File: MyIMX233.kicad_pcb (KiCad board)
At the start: 2 copper layers, 74.1 x 92 mm, 82 parts, among them IC1 iMX233, IC2 DDR_SDRAM_MT46_x16, J1 USB_OTG, P1 4p2, P2 1v2, P3 VDDA1v8, P4 2v5, P5 3v3, P6 1v, SW1 SWITCH_PUSHBUTTON, Y1 24Mhz

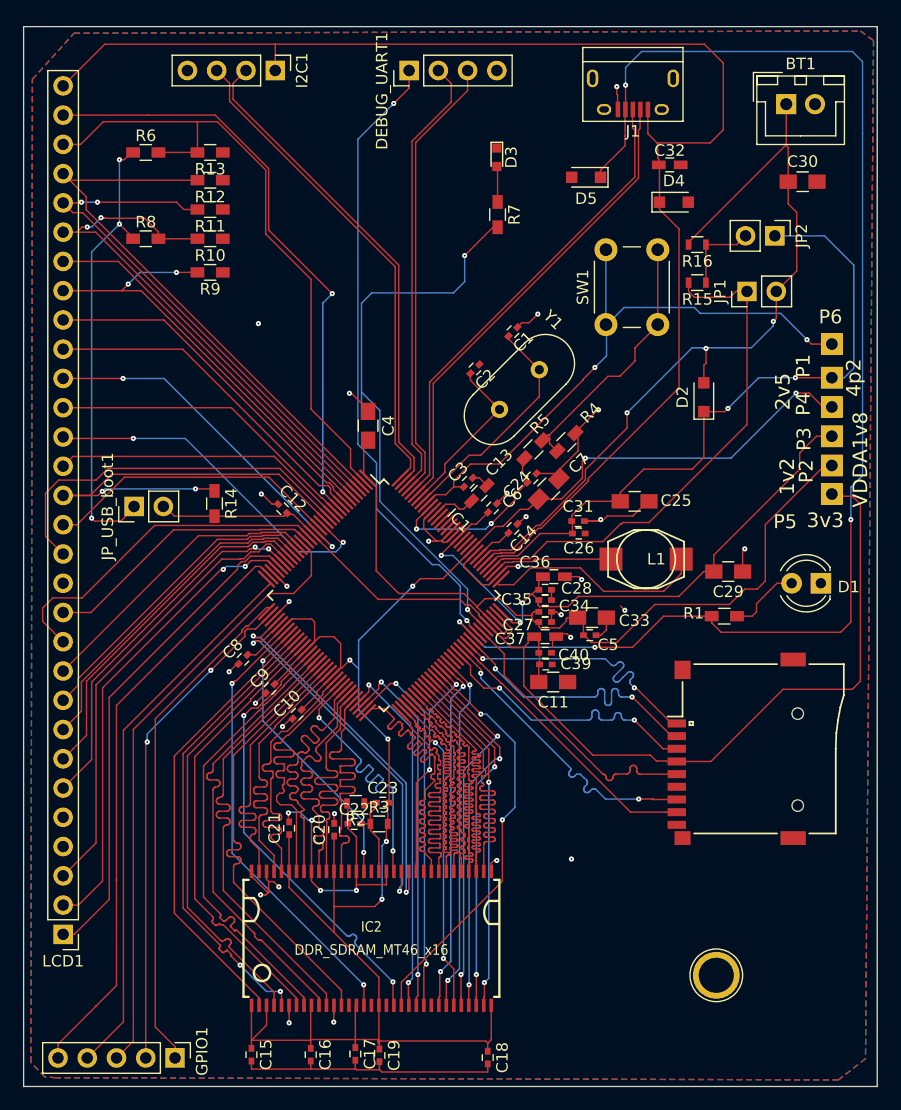
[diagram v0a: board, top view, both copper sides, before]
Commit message: added electrolytic caps and fixed a bug in RAM CS and CE resistors
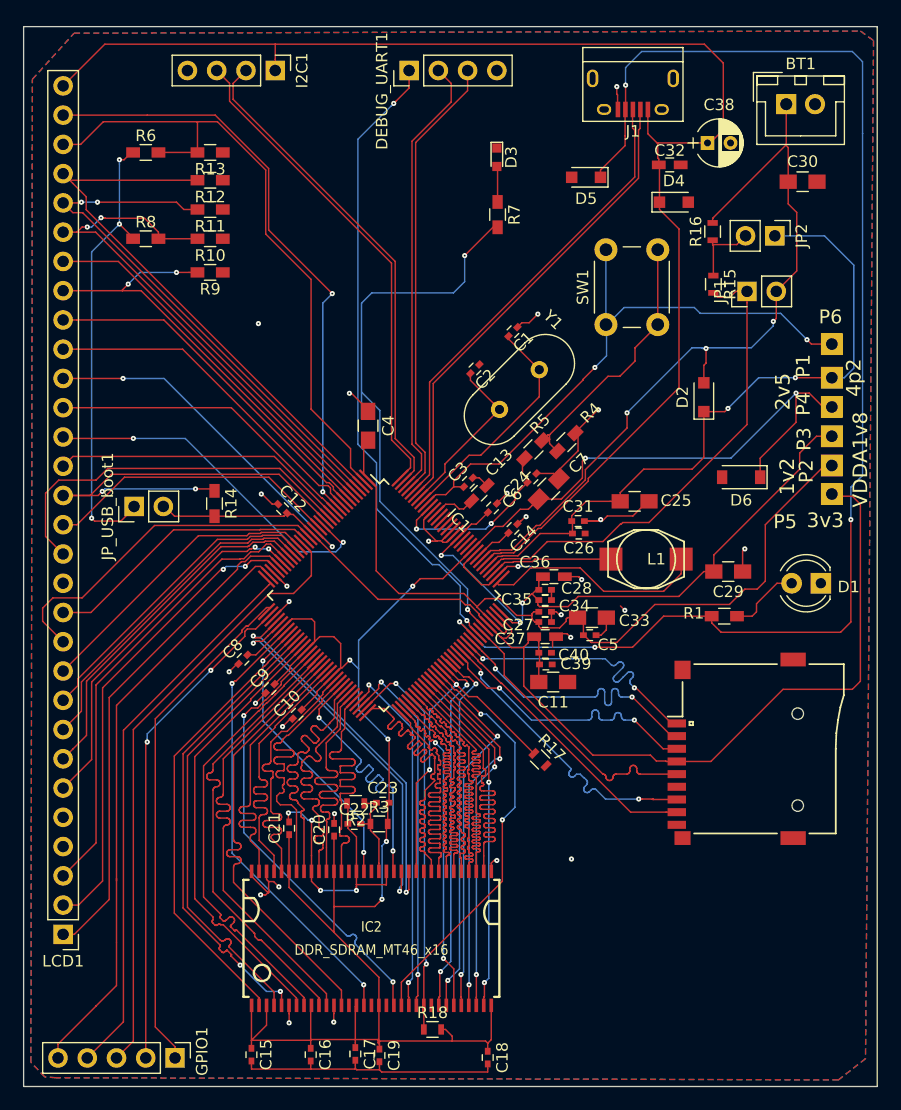
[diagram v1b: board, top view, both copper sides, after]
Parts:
- removed REF**: 1pin, Connectors:1pin
- added C38: 10uF, Capacitors_THT:CP_Radial_D4.0mm_P2.00mm, F.Cu at (125.1, 59.6)
- added D6: 3.3v, Diodes_SMD:D_SOD-123, F.Cu at (128.0, 88.6)
- added R17: 47K, Resistors_SMD:R_0603, F.Cu at (110.6, 113.2)
- added R18: 47K, Resistors_SMD:R_0603, F.Cu at (101.2, 136.6)
- moved R16 1.75 mm to (125.5, 67.3), turned to 90 degrees
- moved R15 1.40 mm to (125.6, 71.9), turned to 270 degrees
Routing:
- net 2V5_SYS: track 176.1 -> 186.3 mm
- net /CKE: track 20.5 -> 29.7 mm
- net /DCDC_BATT: track 45.7 -> 42.7 mm
- net /+VE: track 71.9 -> 69.1 mm
- net /CS: track 32.8 -> 34.9 mm
- net Net-(JP2-Pad2): track 7.06 -> 6.27 mm
- net BA1: track 31.8 -> 32.5 mm
- net BA0: track 30.9 -> 31.5 mm

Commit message: squashed 5 commits
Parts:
- added C41: 1u, Capacitors_SMD:C_0603_HandSoldering, F.Cu at (126.3, 76.1)
- added D10: 5.1v, Diodes_SMD:D_SOD-323_HandSoldering, F.Cu at (135.1, 64.0)
- added D7: 5.1v, Diodes_THT:D_DO-35_SOD27_P7.62mm_Horizontal, F.Cu at (123.8, 64.2)
- added D8: 3.3v, Diodes_THT:D_DO-35_SOD27_P7.62mm_Horizontal, F.Cu at (126.7, 92.8)
- added D9: 5.1v, Diodes_THT:D_DO-35_SOD27_P7.62mm_Horizontal, F.Cu at (111.3, 60.6)
- added R19: 0.1ohm, Resistors_SMD:R_0603_HandSoldering, F.Cu at (126.4, 54.6)
- added REF**: 1pin, Connectors:1pin, F.Cu at (123.3, 131.3)
- C38: footprint Capacitors_THT:CP_Radial_D4.0mm_P2.00mm -> Capacitors_THT:CP_Radial_D5.0mm_P2.50mm
- C7: value 22u -> 1u
- moved R16 11.4 mm to (131.2, 77.2), turned to 180 degrees
- moved R15 6.10 mm to (131.1, 74.5), turned to 180 degrees
- moved C30 3.47 mm to (135.1, 60.0)
- moved BT1 2.82 mm to (133.2, 53.7)
- moved JP1 2.36 mm to (126.6, 71.1), turned to 180 degrees
- moved D4 2.11 mm to (120.1, 65.2), turned to 180 degrees
- moved JP2 1.44 mm to (132.0, 68.6), turned to 0 degrees
- moved C38 0.71 mm to (125.7, 59.3)
- moved DEBUG_UART1 0.38 mm to (99.2, 53.7)
- moved I2C1 0.38 mm to (87.6, 53.7)
- moved C37 0.20 mm to (111.1, 102.7)
- moved C27 0.13 mm to (111.0, 101.3)
- moved C34 0.06 mm to (111.0, 100.4)
- turned C29 to 0 degrees
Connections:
- C38 pad 1: +5V -> Net-(C38-Pad1)
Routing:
- net Net-(C38-Pad1): track 0.00 -> 7.93 mm
- net 2V5_SYS: track 186.3 -> 191.7 mm
- net GND: track 122.6 -> 117.3 mm, vias 32 -> 34
- net USB_ID: track 120.3 -> 125.4 mm
- net /DCDC_BATT: track 42.7 -> 45.2 mm
- net VDDA_SYS: track 56.7 -> 58.2 mm
- net VDDXTAL_SYS: track 53.4 -> 54.7 mm, vias 2 -> 1
- net Net-(IC1-Pad8): track 32.8 -> 31.6 mm
- net +5V: track 123.3 -> 122.1 mm
- net 3v3_SYS: track 102.3 -> 101.2 mm
- net Net-(IC1-Pad20): track 24.9 -> 24.3 mm
- net Net-(C1-Pad2): track 20.8 -> 20.2 mm
- net /+VE: track 69.1 -> 68.5 mm
- net /DCDC_4P2: track 59.8 -> 59.3 mm
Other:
- board text added: "1"
- board text added: "32"
- board text added: "64"
- board text added: "Batt"
- board text added: "Gnd"
- board text added: "No-Batt"
- board text added: "Rx"
- board text added: "Tx"

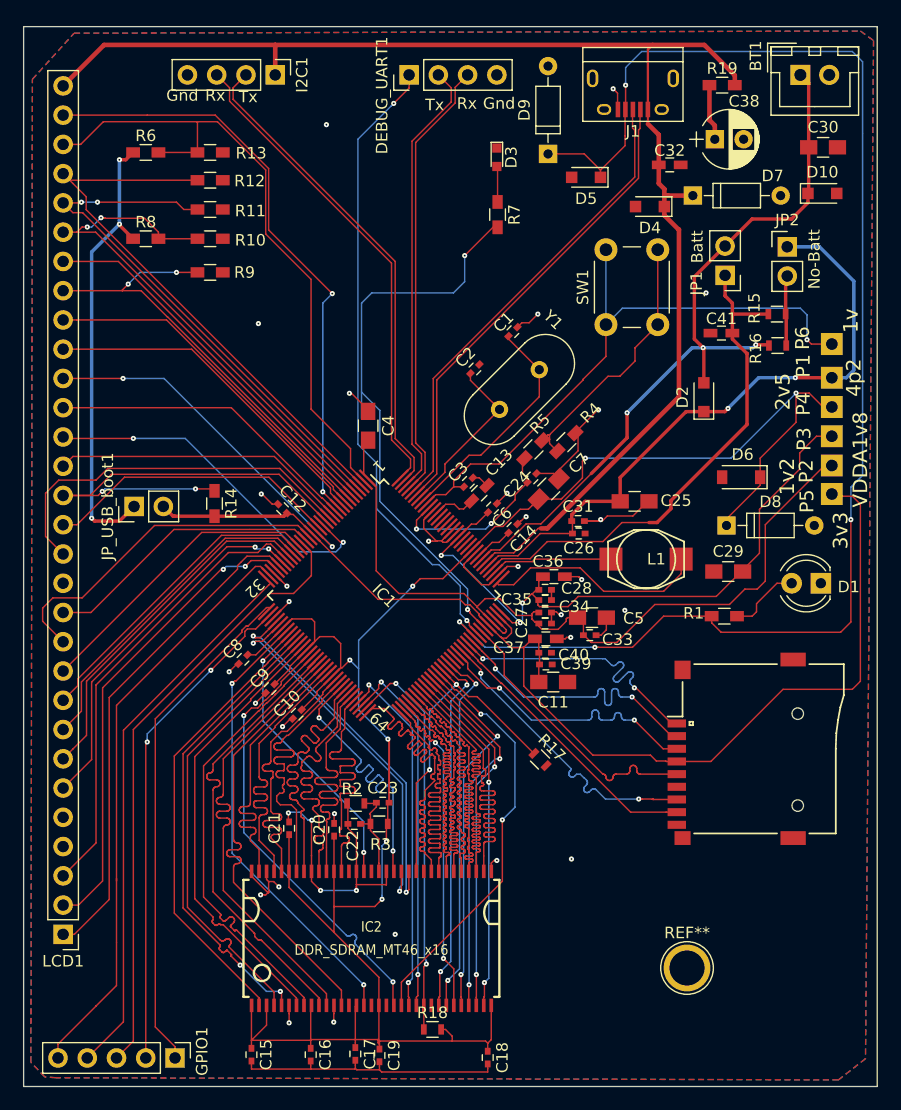
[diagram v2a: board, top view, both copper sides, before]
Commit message: added  SD data resistors, clk nCLK resistor, series resistor to stop oscillation
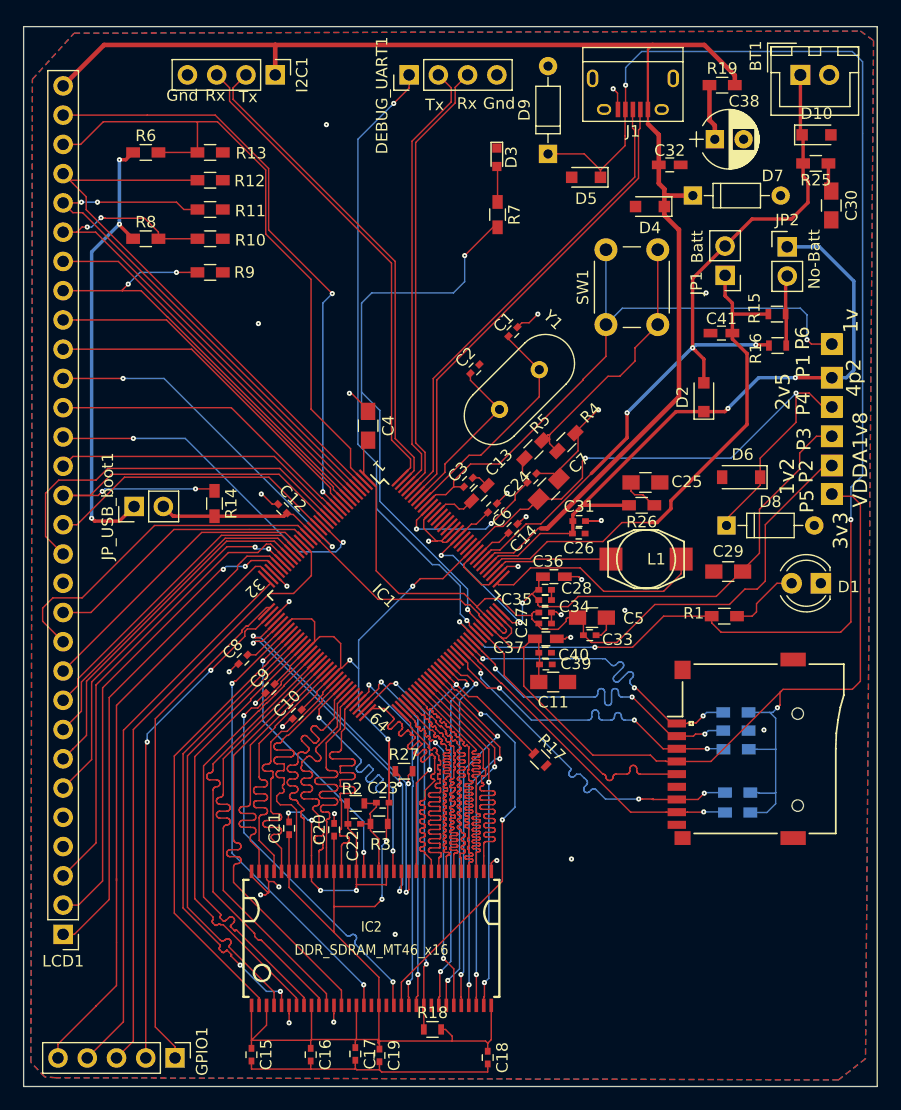
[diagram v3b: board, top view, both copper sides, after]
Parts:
- removed REF**: 1pin, Connectors:1pin
- added R20: 470k, Resistors_SMD:R_0603_HandSoldering, B.Cu at (127.6, 110.6)
- added R21: 100k, Resistors_SMD:R_0603_HandSoldering, B.Cu at (127.7, 116.0)
- added R22: 100k, Resistors_SMD:R_0603_HandSoldering, B.Cu at (127.7, 117.8)
- added R23: 100k, Resistors_SMD:R_0603_HandSoldering, B.Cu at (127.6, 109.1)
- added R24: 10k, Resistors_SMD:R_0603_HandSoldering, B.Cu at (127.6, 112.3)
- added R25: 0.1ohm, Resistors_SMD:R_0603_HandSoldering, F.Cu at (134.5, 61.4)
- added R26: 0.1ohm, Resistors_SMD:R_0603_HandSoldering, F.Cu at (119.4, 91.1)
- added R27: 120R, Resistors_SMD:R_0603, F.Cu at (98.7, 114.2)
- moved D10 5.11 mm to (134.6, 58.9)
- moved C30 5.10 mm to (135.8, 65.1), turned to 270 degrees
- moved C25 1.89 mm to (119.7, 89.1)
- moved C31 0.10 mm to (114.0, 92.5)
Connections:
- C25 pad 2: /DCDC_4P2 -> Net-(C25-Pad2)
- C30 pad 1: /+VE -> Net-(C30-Pad1)
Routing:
- net 3v3_SYS: track 101.2 -> 120.7 mm, vias 0 -> 1
- net GND: track 117.3 -> 112.5 mm, vias 34 -> 35
- net /SD0: track 26.9 -> 31.4 mm, vias 2 -> 3
- net /SD2: track 24.8 -> 29.2 mm, vias 2 -> 3
- net /SD3: track 24.8 -> 29.0 mm, vias 2 -> 3
- net /SD1: track 24.8 -> 29.0 mm, vias 0 -> 1
- net /SD_CMD: track 24.6 -> 28.7 mm, vias 2 -> 3
- net Net-(C25-Pad2): track 0.00 -> 3.29 mm
- net /DCDC_4P2: track 59.3 -> 62.1 mm
- net Net-(C30-Pad1): track 0.00 -> 2.50 mm
- net /CK-: track 32.2 -> 33.8 mm, vias 2 -> 3
- net /CK+: track 32.6 -> 34.1 mm, vias 2 -> 3
- net /+VE: track 68.5 -> 67.5 mm

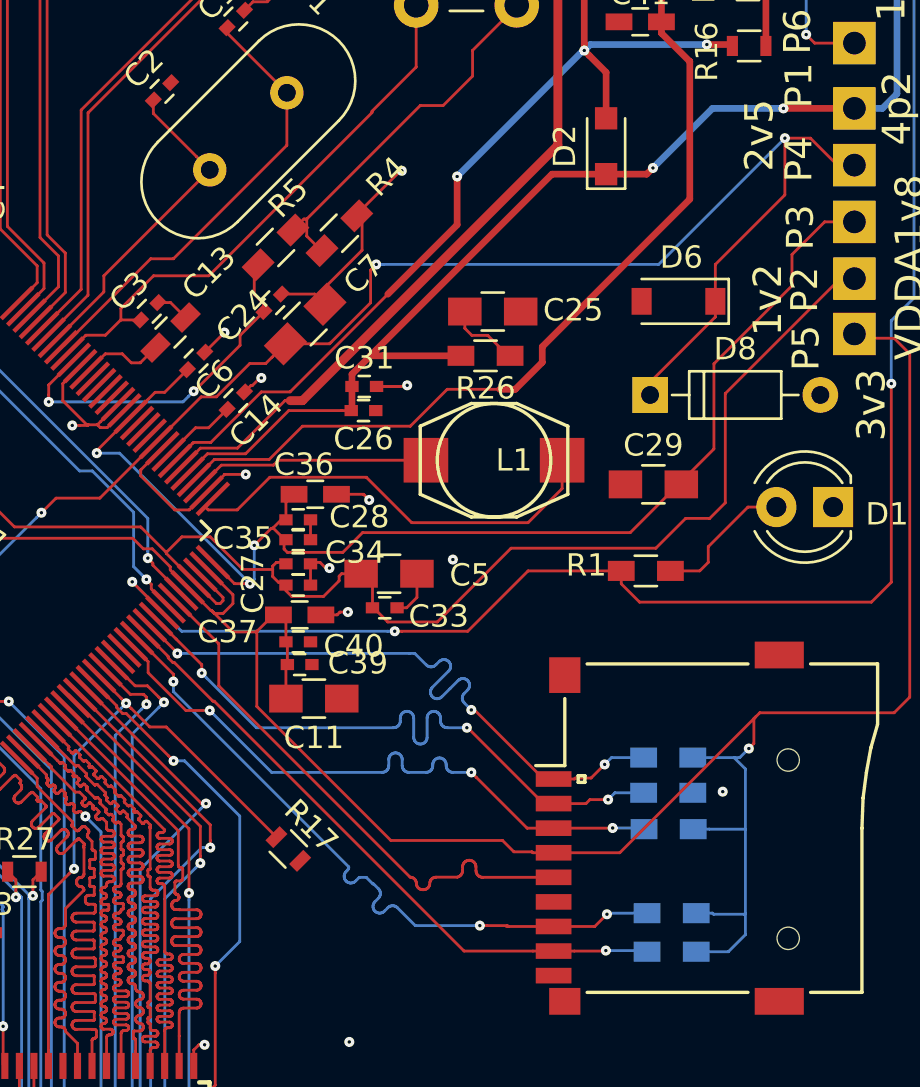
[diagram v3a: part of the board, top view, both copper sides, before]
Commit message: added optional 22uf electrolyte cap in 4p2
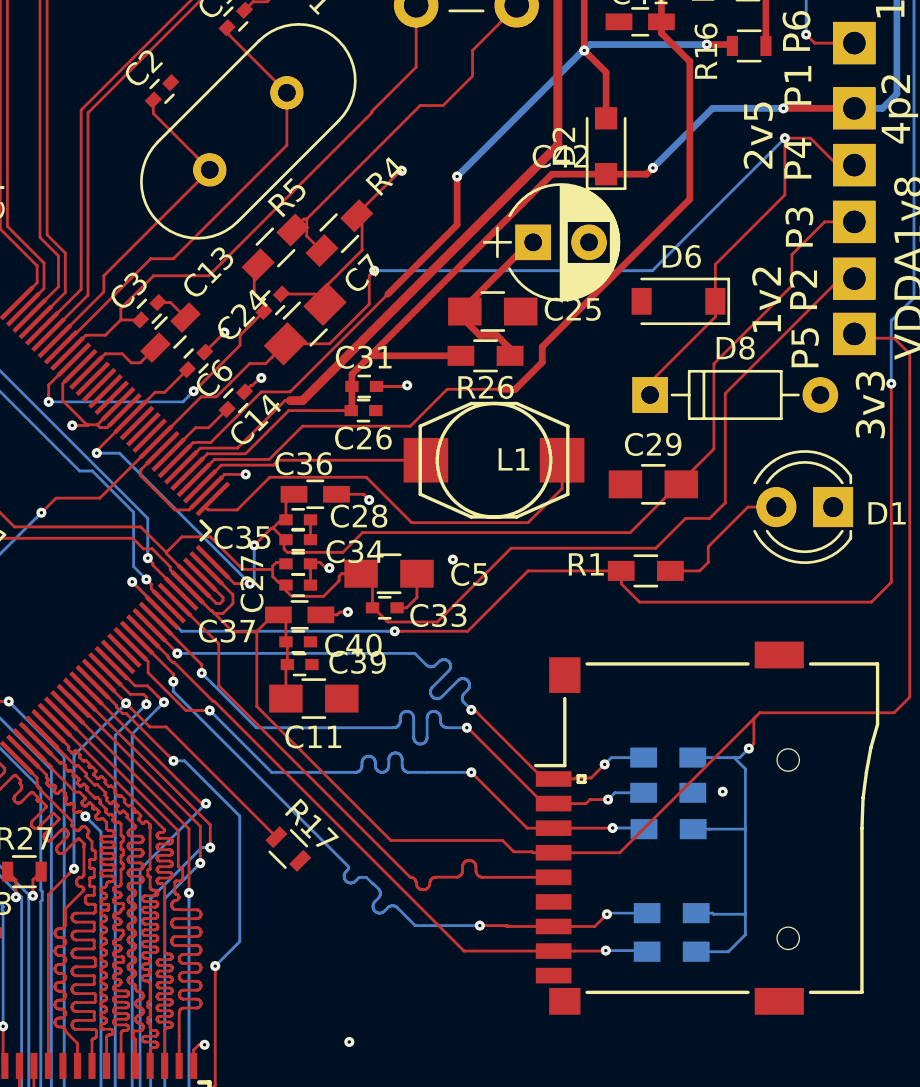
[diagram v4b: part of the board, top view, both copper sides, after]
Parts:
- added C42: 22uF, Capacitors_THT:CP_Radial_D5.0mm_P2.50mm, F.Cu at (121.5, 86.0)
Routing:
- net Net-(C25-Pad2): track 3.29 -> 7.72 mm

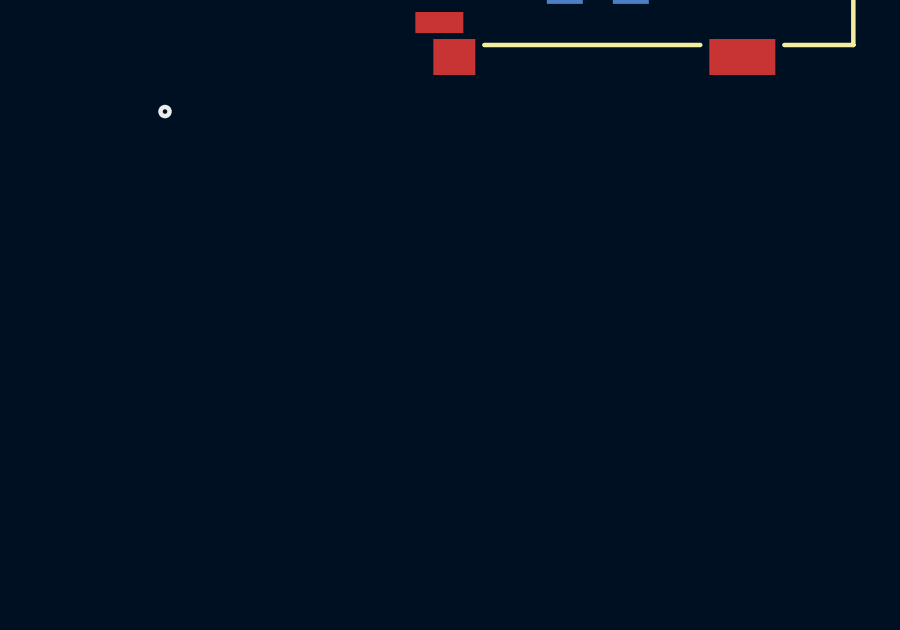
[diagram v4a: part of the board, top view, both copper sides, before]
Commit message: mounting hole added once for all time in schematic
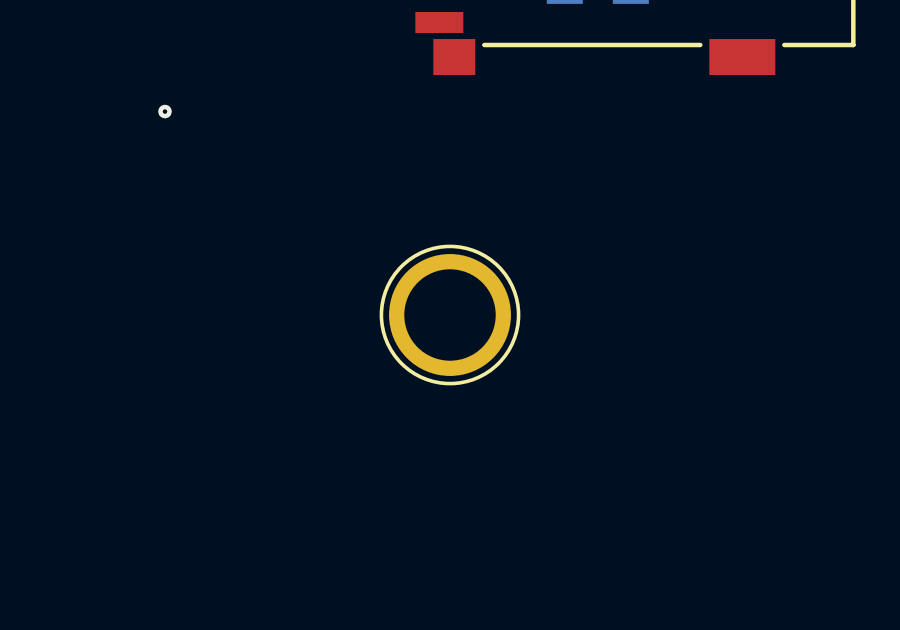
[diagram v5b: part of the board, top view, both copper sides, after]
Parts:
- added J2: CONN_01X01, Connectors:1pin, F.Cu at (122.8, 128.6)
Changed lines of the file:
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@@
     (tracks 7550)
     (zones 0)
-    (modules 100)
+    (modules 101)
     (nets 134)
   )
@@
     (add_net VDDXTAL_SYS)
   )
+  (module Connectors:1pin (layer F.Cu)
+    (at 122.7836 128.5748)
+    (descr "module 1 pin (ou trou mecanique de percage)")
+    (tags DEV)
+    (fp_text reference J2 (at 0 -3.048) (layer F.SilkS) hide
+      (effects (font (size 1 1) (thickness 0.15)))
+    )
+    (fp_text value CONN_01X01 (at 0 3) (layer F.Fab)
+      (effects (font (size 1 1) (thickness 0.15)))
+    )
+    (fp_circle (center 0 0) (end 0 -2.286) (layer F.SilkS) (width 0.12))
+    (fp_circle (center 0 0) (end 2.6 0) (layer F.CrtYd) (width 0.05))
+    (fp_circle (center 0 0) (end 2 0.8) (layer F.Fab) (width 0.1))
+    (pad 1 thru_hole circle (at 0 0) (size 4.064 4.064) (drill 3.048) (layers *.Cu *.Mask)
+      (net 2 GND))
+  )
   (module Capacitors_THT:CP_Radial_D5.0mm_P2.50mm (layer F.Cu)
